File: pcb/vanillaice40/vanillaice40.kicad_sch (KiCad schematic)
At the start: 105 parts, among them J1 FX18-120S-0.8SV20, J2 SM04B-SRSS-TBLFSN, J3 SM04B-SRSS-TBLFSN, SW1 USR1, SW2 USR1, SW3 RESET, U1 TPS563252DRLR, U2 ICE40HX4K-TQ144, U3 W25X40CLSN, U4 TPS563252DRLR, U5 FT2232HL, U6 93LCxxBxxOT, X1 SG-8101CE 100Mhz, Y1 12Mhz/18pf

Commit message: rough pcb placement done
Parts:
- removed J3: SM04B-SRSS-TBLFSN, CONN_SM04B_JST, symbol SM04B-SRSS-TB-LF-SN:SM04B-SRSS-TBLFSN
- added D6, D7: Red, Diode_SMD:D_0603_1608Metric, symbol Device:LED_Small
- added R38, R39: 2.2k, Resistor_SMD:R_0603_1608Metric, symbol Device:R_Small
- D4: value Green -> Red
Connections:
- net +1V2: now also R38.1
- net +3V3: now also R6.2, R39.1; no longer X1.1 (OE)
- net GND: now also D6.1 (K), D7.1 (K)
- net IOL_14A: now also X1.3 (OUT); no longer R6.2
- net at R6.1: now also X1.1 (OE); no longer X1.3 (OUT)
- new net: D7.2 (A), R39.2
- new net: D6.2 (A), R38.2
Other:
- moved on the sheet: C1, J2

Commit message: drc constraints
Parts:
- added J3: Conn_01x02_Pin, Connector_PinHeader_2.54mm:PinHeader_1x02_P2.54mm_Vertical, symbol Connector:Conn_01x02_Pin
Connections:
- net GND: now also J3.2 (Pin_2)
- net at FB1.1, USB1.A4 (VBUS), USB1.A9 (VBUS)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: now also J3.1 (Pin_1)
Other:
- moved on the sheet: C13, D4, FB1, R10, R13, R5, R9, SW3, USB1

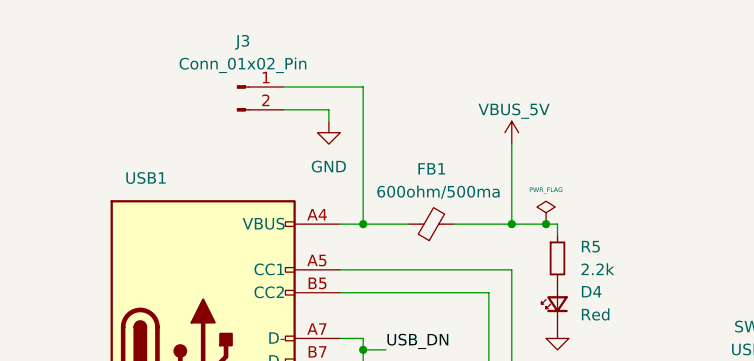
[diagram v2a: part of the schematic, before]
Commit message: usb power routing
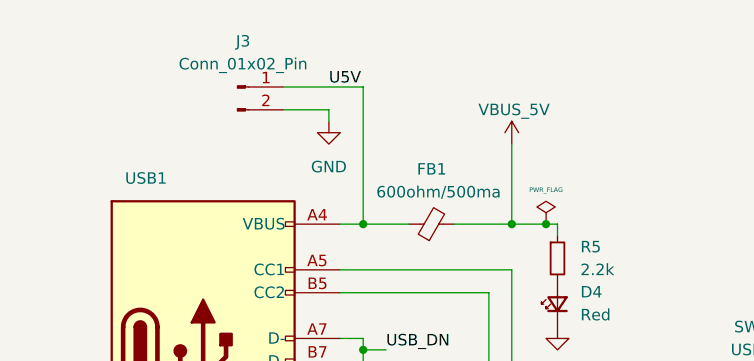
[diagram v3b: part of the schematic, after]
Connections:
- net U5V: now reaches FB1.1, J3.1 (Pin_1), USB1.A4 (VBUS), USB1.A9 (VBUS), USB1.B4 (VBUS), USB1.B9 (VBUS)
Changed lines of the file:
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@@
+		)
+	)
+	(label "U5V"
+		(at 49.53 22.86 0)
+		(fields_autoplaced yes)
+		(effects
+			(font
+				(size 1.27 1.27)
+			)
+			(justify left bottom)
 		)
 	)

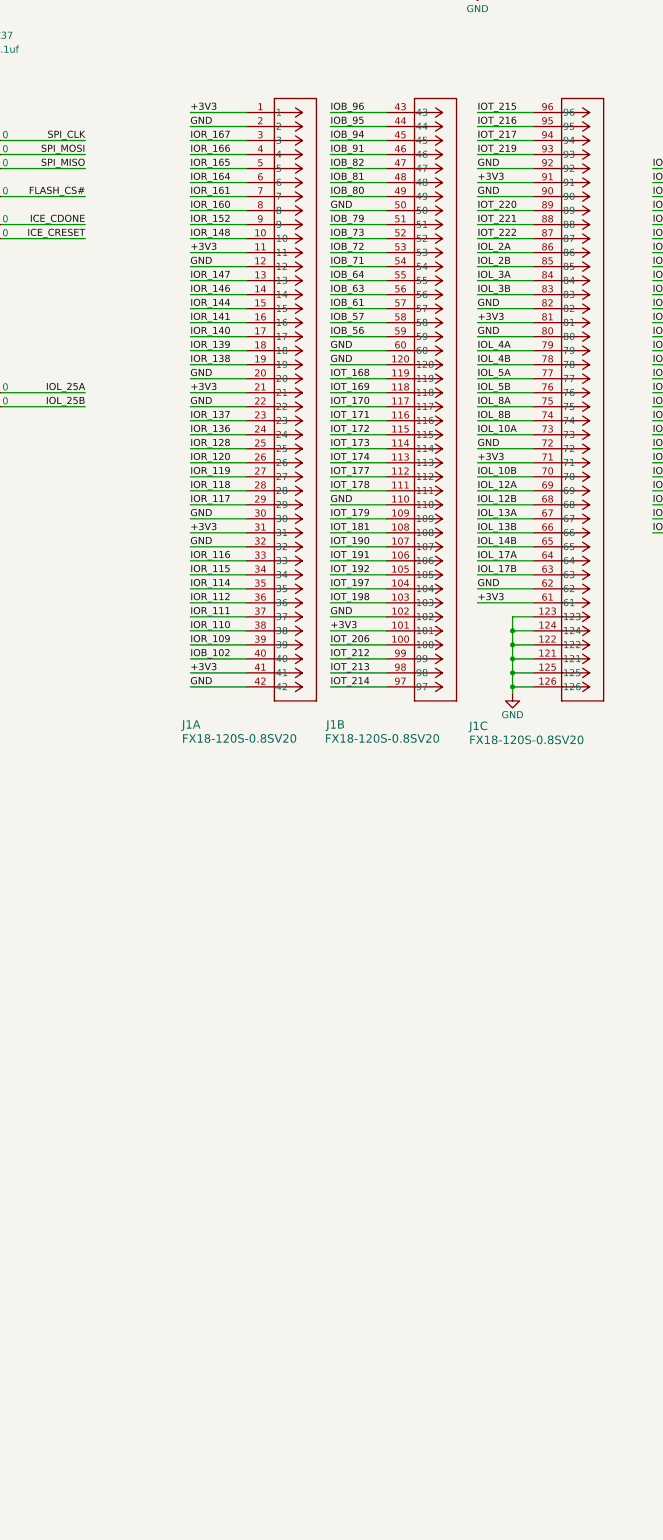
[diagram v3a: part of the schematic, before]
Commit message: schematic breakout cleared
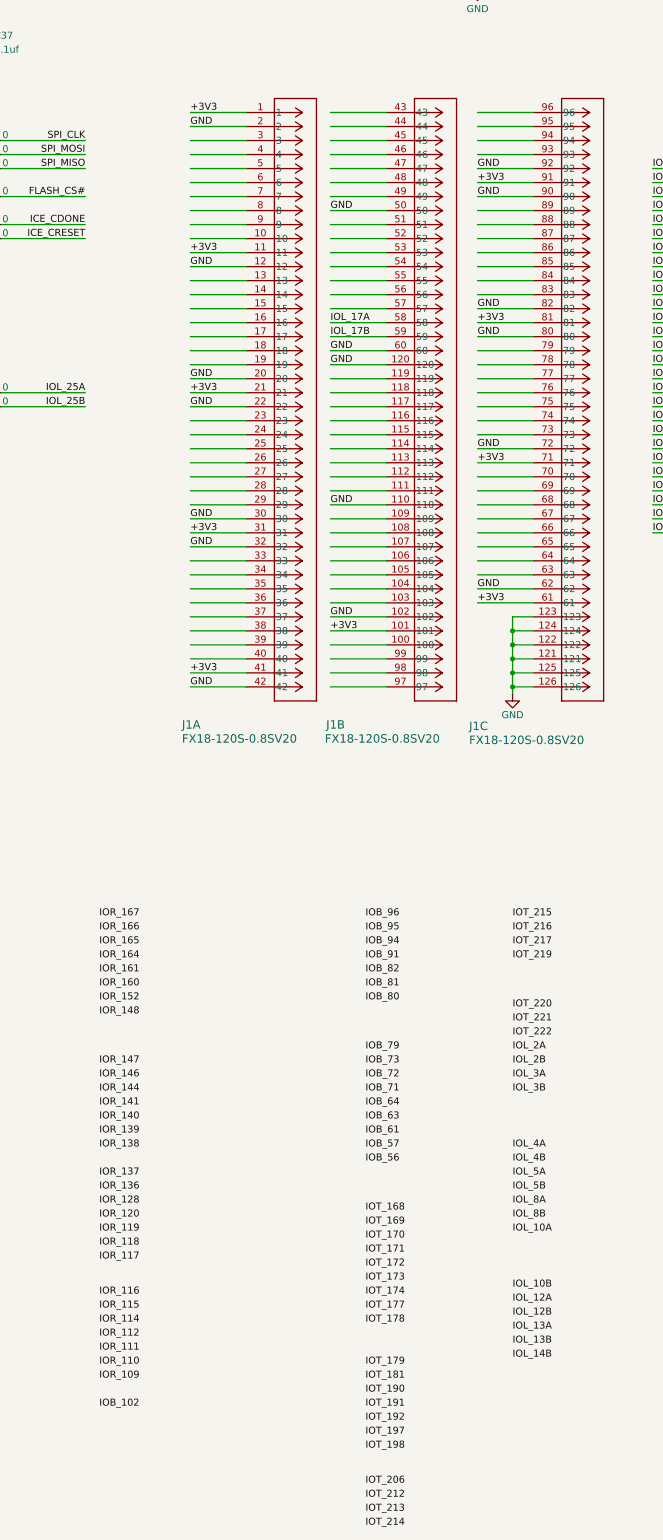
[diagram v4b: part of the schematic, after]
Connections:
- net IOB_102: no longer J1.40
- net IOB_56: no longer J1.59
- net IOB_57: no longer J1.58
- net IOB_61: no longer J1.57
- net IOB_63: no longer J1.56
- net IOB_64: no longer J1.55
- net IOB_71: no longer J1.54
- net IOB_72: no longer J1.53
- net IOB_73: no longer J1.52
- net IOB_79: no longer J1.51
- net IOB_80: no longer J1.49
- net IOB_81: no longer J1.48
- net IOB_82: no longer J1.47
- net IOB_91: no longer J1.46
- net IOB_94: no longer J1.45
- net IOB_95: no longer J1.44
- net IOB_96: no longer J1.43
- net IOL_10A: no longer J1.73
- net IOL_10B: no longer J1.70
- net IOL_12A: no longer J1.69
- net IOL_12B: no longer J1.68
- net IOL_13A: no longer J1.67
- net IOL_13B: no longer J1.66
- net IOL_14B: no longer J1.65
- net IOL_17A: now also J1.58; no longer J1.64
- net IOL_17B: now also J1.59; no longer J1.63
- net IOL_2A: no longer J1.86
- net IOL_2B: no longer J1.85
- net IOL_3A: no longer J1.84
- net IOL_3B: no longer J1.83
- net IOL_4A: no longer J1.79
- net IOL_4B: no longer J1.78
- net IOL_5A: no longer J1.77
- net IOL_5B: no longer J1.76
- net IOL_8A: no longer J1.75
- net IOL_8B: no longer J1.74
- net IOR_109: no longer J1.39
- net IOR_110: no longer J1.38
- net IOR_111: no longer J1.37
- net IOR_112: no longer J1.36
- net IOR_114: no longer J1.35
- net IOR_115: no longer J1.34
- net IOR_116: no longer J1.33
- net IOR_117: no longer J1.29
- net IOR_118: no longer J1.28
- net IOR_119: no longer J1.27
- net IOR_120: no longer J1.26
- net IOR_128: no longer J1.25
- net IOR_136: no longer J1.24
- net IOR_137: no longer J1.23
- net IOR_138: no longer J1.19
- net IOR_139: no longer J1.18
- net IOR_140: no longer J1.17
- net IOR_141: no longer J1.16
- net IOR_144: no longer J1.15
- net IOR_146: no longer J1.14
- net IOR_147: no longer J1.13
- net IOR_148: no longer J1.10
- net IOR_152: no longer J1.9
- net IOR_160: no longer J1.8
- net IOR_161: no longer J1.7
- net IOR_164: no longer J1.6
- net IOR_165: no longer J1.5
- net IOR_166: no longer J1.4
- net IOR_167: no longer J1.3
- net IOT_168: no longer J1.119
- net IOT_169: no longer J1.118
- net IOT_170: no longer J1.117
- net IOT_171: no longer J1.116
- net IOT_172: no longer J1.115
- net IOT_173: no longer J1.114
- net IOT_174: no longer J1.113
- net IOT_177: no longer J1.112
- net IOT_178: no longer J1.111
- net IOT_179: no longer J1.109
- net IOT_181: no longer J1.108
- net IOT_190: no longer J1.107
- net IOT_191: no longer J1.106
- net IOT_192: no longer J1.105
- net IOT_197: no longer J1.104
- net IOT_198: no longer J1.103
- net IOT_206: no longer J1.100
- net IOT_212: no longer J1.99
- net IOT_213: no longer J1.98
- net IOT_214: no longer J1.97
- net IOT_215: no longer J1.96
- net IOT_216: no longer J1.95
- net IOT_217: no longer J1.94
- net IOT_219: no longer J1.93
- net IOT_220: no longer J1.89
- net IOT_221: no longer J1.88
- net IOT_222: no longer J1.87

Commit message: io moved to lower diff
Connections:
- net +3V3: no longer J1.101, J1.11, J1.21, J1.31, J1.41, J1.71, J1.81, J1.91
- net GND: no longer J1.102, J1.110, J1.12, J1.120, J1.20, J1.22, J1.30, J1.32, J1.42, J1.50, J1.60, J1.72, J1.80, J1.82, J1.90, J1.92
- net IOL_17A: no longer J1.58
- net IOL_17B: no longer J1.59
- net IOL_18A: no longer R7.2, SW1.2
- net IOL_18B: no longer R8.2, SW2.2
- net IOL_23A: no longer J2.1
- net IOL_23B: no longer J2.2
- net IOL_24A: no longer R1.1
- net IOL_24B: no longer R2.1
- net IOL_25A: no longer R32.2
- net IOL_25B: no longer R33.2
- net IOL_2A: now also R1.1
- net IOL_2B: now also R2.1
- net IOL_3A: now also R7.2, SW1.2
- net IOL_3B: now also R8.2, SW2.2
- net IOL_4A: now also R32.2
- net IOL_4B: now also R33.2
- net IOL_5A: now also J2.1
- net IOL_5B: now also J2.2

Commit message: fx18 power redo
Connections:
- net +3V3: now also J1.109, J1.11, J1.119, J1.21, J1.39, J1.49, J1.59, J1.70, J1.80, J1.99
- net GND: now also J1.100, J1.110, J1.12, J1.120, J1.22, J1.40, J1.50, J1.60, J1.71, J1.81
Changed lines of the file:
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@@
+		)
+	)
+	(label "GND"
+		(at 201.93 200.66 0)
+		(fields_autoplaced yes)
+		(effects
+			(font
+				(size 1.27 1.27)
+			)
+			(justify left bottom)
 		)
 	)
@@
 	)
 	(label "GND"
-		(at 180.34 222.25 0)
+		(at 201.93 246.38 0)
 		(fields_autoplaced yes)
 		(effects
@@
 	)
 	(label "+3V3"
-		(at 180.34 228.6 0)
+		(at 227.33 162.56 0)
 		(fields_autoplaced yes)
 		(effects
@@
 		)
 	)
+	(label "+3V3"
+		(at 227.33 246.38 0)
+		(fields_autoplaced yes)
+		(effects
+			(font
+				(size 1.27 1.27)
+			)
+			(justify left bottom)
+		)
+	)
 	(label "IOR_139"
 		(at 185.42 332.74 0)
@@
 		)
 	)
+	(label "GND"
+		(at 227.33 218.44 0)
+		(fields_autoplaced yes)
+		(effects
+			(font
+				(size 1.27 1.27)
+			)
+			(justify left bottom)
+		)
+	)
 	(label "ICE_CRESET"
 		(at 182.88 170.18 180)
@@
 		)
 	)
+	(label "+3V3"
+		(at 254 187.96 0)
+		(fields_autoplaced yes)
+		(effects
+			(font
+				(size 1.27 1.27)
+			)
+			(justify left bottom)
+		)
+	)
 	(label "SPI_MOSI"
 		(at 127 92.71 0)
@@
 		)
 	)
+	(label "+3V3"
+		(at 254 236.22 0)
+		(fields_autoplaced yes)
+		(effects
+			(font
+				(size 1.27 1.27)
+			)
+			(justify left bottom)
+		)
+	)
 	(label "FLASH_CS#"
 		(at 127 87.63 0)
@@
 	)
 	(label "+3V3"
-		(at 181.61 240.03 0)
+		(at 227.33 187.96 0)
 		(fields_autoplaced yes)
 		(effects
@@
 		)
 	)
+	(label "+3V3"
+		(at 201.93 172.72 0)
+		(fields_autoplaced yes)
+		(effects
+			(font
+				(size 1.27 1.27)
+			)
+			(justify left bottom)
+		)
+	)
 	(label "IOT_191"
 		(at 285.75 187.96 0)
@@
 		)
 	)
+	(label "+3V3"
+		(at 254 213.36 0)
+		(fields_autoplaced yes)
+		(effects
+			(font
+				(size 1.27 1.27)
+			)
+			(justify left bottom)
+		)
+	)
 	(label "IOT_169"
 		(at 233.68 349.25 0)
@@
 		)
 	)
+	(label "+3V3"
+		(at 227.33 220.98 0)
+		(fields_autoplaced yes)
+		(effects
+			(font
+				(size 1.27 1.27)
+			)
+			(justify left bottom)
+		)
+	)
 	(label "IOR_111"
 		(at 320.04 157.48 0)
@@
 	)
 	(label "+3V3"
-		(at 180.34 219.71 0)
+		(at 201.93 243.84 0)
 		(fields_autoplaced yes)
 		(effects
@@
 	)
 	(label "GND"
-		(at 181.61 237.49 0)
+		(at 227.33 190.5 0)
 		(fields_autoplaced yes)
 		(effects
@@
 		)
 	)
+	(label "GND"
+		(at 254 185.42 0)
+		(fields_autoplaced yes)
+		(effects
+			(font
+				(size 1.27 1.27)
+			)
+			(justify left bottom)
+		)
+	)
 	(label "IOT_198"
 		(at 285.75 195.58 0)
@@
 		)
 	)
+	(label "GND"
+		(at 201.93 175.26 0)
+		(fields_autoplaced yes)
+		(effects
+			(font
+				(size 1.27 1.27)
+			)
+			(justify left bottom)
+		)
+	)
 	(label "IOT_168"
 		(at 285.75 157.48 0)
@@
 		)
 	)
+	(label "+3V3"
+		(at 201.93 198.12 0)
+		(fields_autoplaced yes)
+		(effects
+			(font
+				(size 1.27 1.27)
+			)
+			(justify left bottom)
+		)
+	)
 	(label "IOL_8B"
 		(at 384.81 177.8 0)
@@
 		)
 	)
+	(label "GND"
+		(at 227.33 243.84 0)
+		(fields_autoplaced yes)
+		(effects
+			(font
+				(size 1.27 1.27)
+			)
+			(justify left bottom)
+		)
+	)
 	(label "IOL_14B"
 		(at 260.35 373.38 0)
@@
 	)
 	(label "GND"
-		(at 180.34 231.14 0)
+		(at 227.33 165.1 0)
 		(fields_autoplaced yes)
 		(effects
@@
 		)
 	)
+	(label "GND"
+		(at 254 233.68 0)
+		(fields_autoplaced yes)
+		(effects
+			(font
+				(size 1.27 1.27)
+			)
+			(justify left bottom)
+		)
+	)
 	(label "USB_DN"
 		(at 86.36 177.8 0)
@@
 	)
 	(label "GND"
-		(at 254 233.68 0)
+		(at 227.33 193.04 0)
 		(fields_autoplaced yes)
 		(effects
@@
 		)
 	)
+	(label "GND"
+		(at 254 210.82 0)
+		(fields_autoplaced yes)
+		(effects
+			(font
+				(size 1.27 1.27)
+			)
+			(justify left bottom)
+		)
+	)
 	(label "IOL_18B"
 		(at 274.32 386.08 0)
@@
 	)
 	(label "+3V3"
-		(at 254 236.22 0)
-		(fields_autoplaced yes)
-		(effects
+		(at 227.33 195.58 0)
+		(fields_autoplaced yes)
+		(effects

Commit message: start of 3rd reroute
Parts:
- removed R7, R8: 10k, Resistor_SMD:R_0603_1608Metric, symbol Device:R_Small
- removed SW1, SW2: USR1, Button_Switch_SMD:SW_SPST_PTS810, symbol Switch:SW_Push
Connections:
- net IOB_102: now also J1.98
- net IOB_56: now also J1.118
- net IOB_57: now also J1.117
- net IOB_61: now also J1.116
- net IOB_63: now also J1.115
- net IOB_64: now also J1.114
- net IOB_71: now also J1.113
- net IOB_72: now also J1.112
- net IOB_73: now also J1.111
- net IOB_79: now also J1.108
- net IOB_80: now also J1.107
- net IOB_81: now also J1.106
- net IOB_82: now also J1.105
- net IOB_91: now also J1.104
- net IOB_94: now also J1.103
- net IOB_95: now also J1.102
- net IOB_96: now also J1.101
- net IOL_10A: now also J1.38
- net IOL_10B: now also J1.41
- net IOL_12A: now also J1.42
- net IOL_12B: now also J1.43
- net IOL_13A: now also J1.44
- net IOL_13B: now also J1.45
- net IOL_14B: now also J1.46
- net IOL_17A: now also J1.47
- net IOL_17B: now also J1.48
- net IOL_18A: now also J1.51
- net IOL_18B: now also J1.52
- net IOL_23A: now also J1.53
- net IOL_23B: now also J1.54
- net IOL_24A: now also J1.55
- net IOL_24B: now also J1.56
- net IOL_25A: now also J1.57
- net IOL_25B: now also J1.58
- net IOL_3A: now also R32.2
- net IOL_3B: now also R33.2
- net IOL_4A: now also J1.32, J2.1; no longer R32.2
- net IOL_4B: now also J1.33, J2.2; no longer R33.2
- net IOL_5A: now also J1.34; no longer J2.1
- net IOL_5B: now also J1.35; no longer J2.2
- net IOL_8A: now also J1.36
- net IOL_8B: now also J1.37
- net IOR_109: now also J1.97
- net IOR_110: now also J1.96
- net IOR_111: now also J1.95
- net IOR_112: now also J1.94
- net IOR_114: now also J1.93
- net IOR_115: now also J1.92
- net IOR_116: now also J1.91
- net IOR_117: now also J1.90
- net IOR_118: now also J1.89
- net IOR_119: now also J1.88
- net IOR_120: now also J1.87
- net IOR_128: now also J1.86
- net IOR_136: now also J1.85
- net IOR_137: now also J1.84
- net IOR_138: now also J1.83
- net IOR_139: now also J1.82
- net IOR_140: now also J1.79
- net IOR_141: now also J1.78
- net IOR_144: now also J1.77
- net IOR_146: now also J1.76
- net IOR_147: now also J1.75
- net IOR_148: now also J1.74
- net IOR_152: now also J1.73
- net IOR_160: now also J1.72
- net IOR_161: now also J1.69
- net IOR_164: now also J1.68
- net IOR_165: now also J1.67
- net IOR_166: now also J1.66
- net IOR_167: now also J1.65
- net IOT_168: now also J1.64
- net IOT_169: now also J1.63
- net IOT_170: now also J1.3
- net IOT_171: now also J1.4
- net IOT_172: now also J1.5
- net IOT_173: now also J1.6
- net IOT_174: now also J1.7
- net IOT_177: now also J1.8
- net IOT_178: now also J1.9
- net IOT_179: now also J1.10
- net IOT_181: now also J1.13
- net IOT_190: now also J1.14
- net IOT_191: now also J1.15
- net IOT_192: now also J1.16
- net IOT_197: now also J1.17
- net IOT_198: now also J1.18
- net IOT_206: now also J1.19
- net IOT_212: now also J1.20
- net IOT_213: now also J1.23
- net IOT_214: now also J1.24
- net IOT_215: now also J1.25
- net IOT_216: now also J1.26
- net IOT_217: now also J1.27
- net IOT_219: now also J1.28
- net IOT_220: now also J1.29
- net IOT_221: now also J1.30
- net IOT_222: now also J1.31
